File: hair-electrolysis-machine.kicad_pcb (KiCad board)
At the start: 2 copper layers, 53 x 53 mm, 84 parts, among them J1 USB_C_Receptacle_USB2.0_16P, J2 Conn_01x04_Pin, J3 AudioJack2_Ground_Switch, J4 AudioJack2_Ground_Switch, J5 Conn_01x04_Pin, J6 Conn_01x04_Pin, J7 AudioJack2_Ground_Switch, Q2 BSS138, SW3 SW_SPDT, SW4 RotaryEncoder_Switch, SW7 TRIGGER, SW8 TRIGGER, SW9 TRIGGER, U1 STM32G0B1RETx, U2 TP4054, U4 XC6206PxxxMR, U8 LM358B

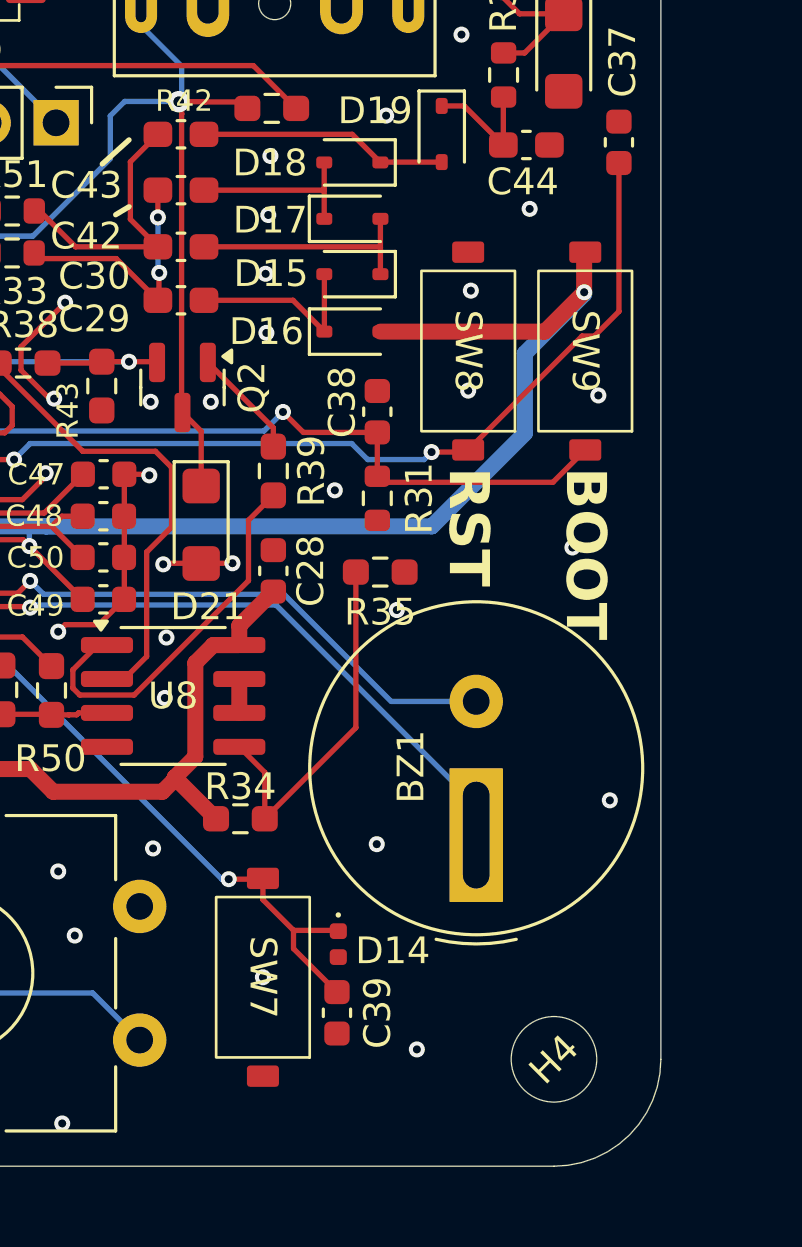
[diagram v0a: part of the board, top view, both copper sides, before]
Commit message: Fix C37 LCSC code, changed buttons to C720477
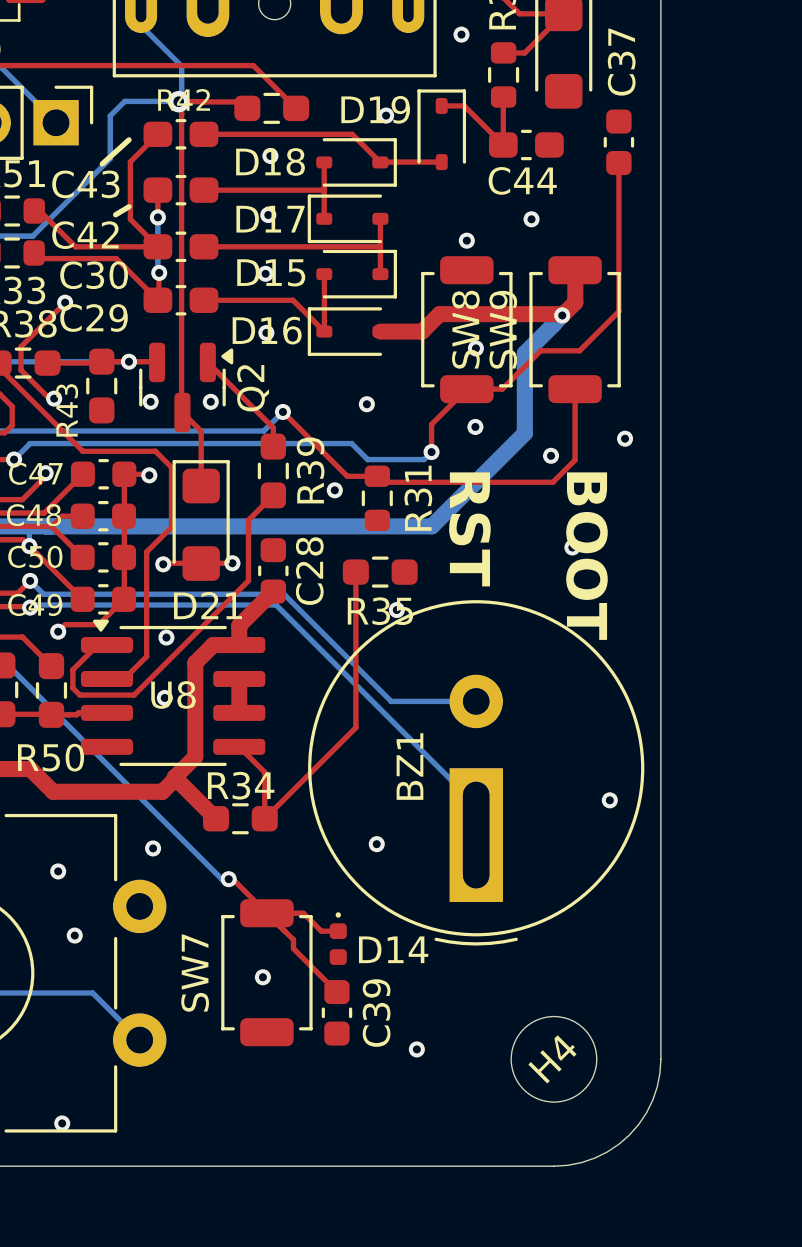
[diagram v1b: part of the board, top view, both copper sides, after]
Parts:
- removed C38: 100nF, Capacitor_SMD:C_0603_1608Metric
- SW7: footprint Button_Switch_SMD:YZA-032-5.0W -> Button_Switch_SMD:SW_SPST_TS-1088-xR025
- SW8: value TRIGGER -> RST; footprint Button_Switch_SMD:YZA-032-5.0W -> Button_Switch_SMD:SW_SPST_TS-1088-xR025
- SW9: value TRIGGER -> BOOT; footprint Button_Switch_SMD:YZA-032-5.0W -> Button_Switch_SMD:SW_SPST_TS-1088-xR025
- moved SW9 0.89 mm to (172.8, 92.7), turned to 90 degrees
- moved SW8 0.80 mm to (168.7, 92.7), turned to 90 degrees
- moved SW7 0.23 mm to (161.3, 116.8), turned to 90 degrees
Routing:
- net +3.3V: track 110.8 -> 108.8 mm
- net /Mcu/TRIGGER: track 66.0 -> 67.5 mm
- net SWCLK: track 51.5 -> 52.6 mm
- net /Mcu/~{RESET}: track 32.4 -> 33.0 mm
- net GND: vias 83 -> 86

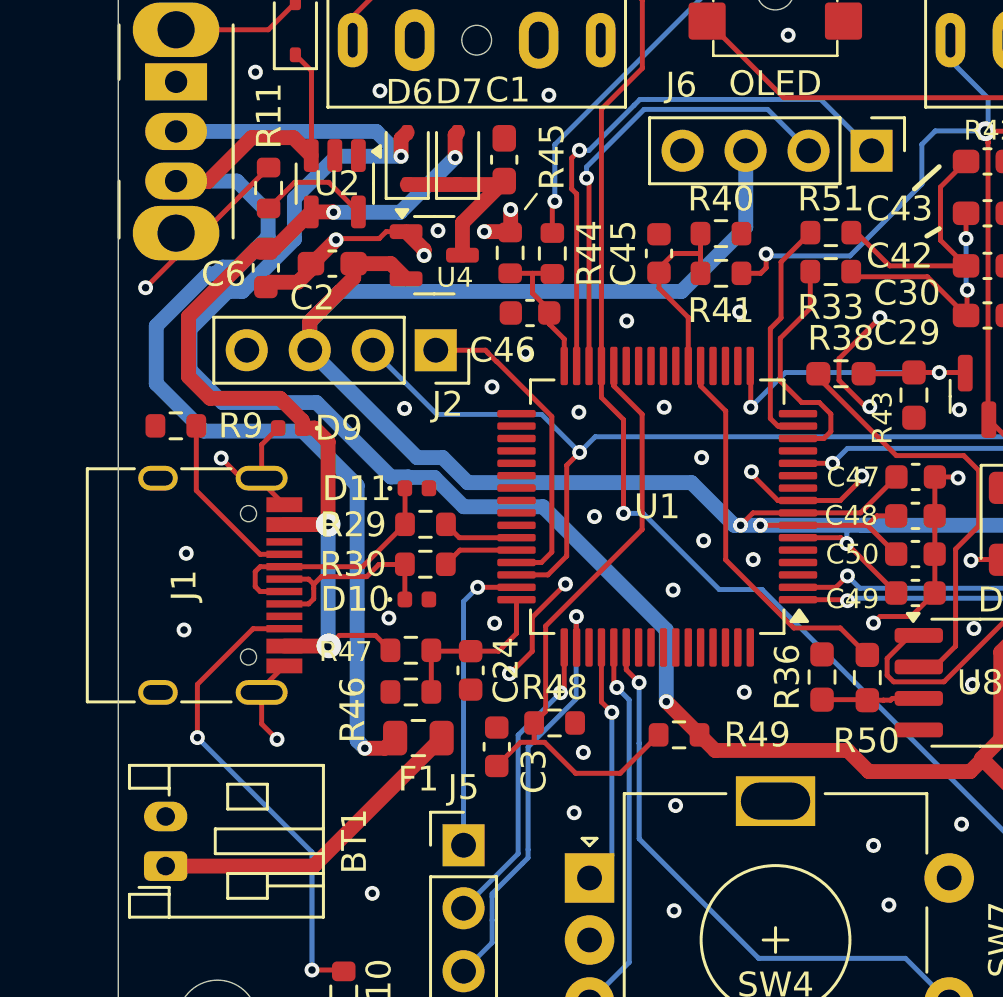
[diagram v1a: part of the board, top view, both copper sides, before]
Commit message: Removed USB resistors, shuffled breakout pins to tidy up a tad
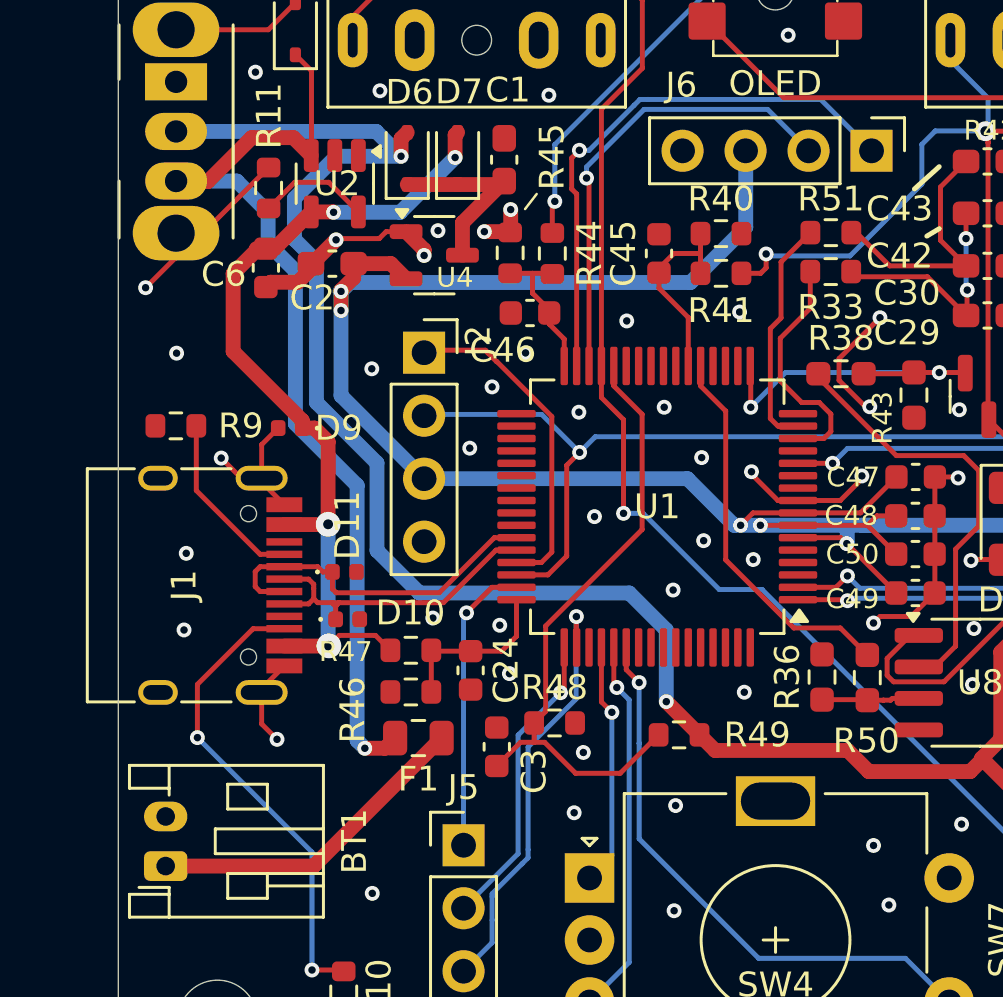
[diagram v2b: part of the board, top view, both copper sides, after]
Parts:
- removed R29, R30: 22R, Resistor_SMD:R_0603_1608Metric
- moved D11 4.46 mm to (132.1, 101.9)
- moved D10 2.90 mm to (132.2, 103.8)
- moved J2 0.48 mm to (135.3, 93.1), turned to 0 degrees
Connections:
- SW3 pad : GND -> (no net)
- U1 pad 43: Net-(U1-PA9/PA11) -> /Mcu/D-
- U1 pad 44: Net-(U1-PA10/PA12) -> /Mcu/D+
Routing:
- net Net-(D5-K): track 45.7 -> 39.1 mm
- net /Mcu/D+: track 8.56 -> 13.2 mm
- net GND: track 58.2 -> 53.6 mm, vias 86 -> 87
- net /Mcu/D-: track 10.2 -> 14.2 mm
- net +BATT: track 75.8 -> 71.8 mm
- net SWCLK: track 52.6 -> 49.5 mm
- net Net-(U1-PA10/PA12): track 3.09 -> 0.00 mm
- net Net-(U1-PA9/PA11): track 3.07 -> 0.00 mm
- net +3.3V: track 108.8 -> 106.0 mm, vias 4 -> 6
- net +5V: track 38.8 -> 36.0 mm
- net SWDIO: track 12.9 -> 13.4 mm

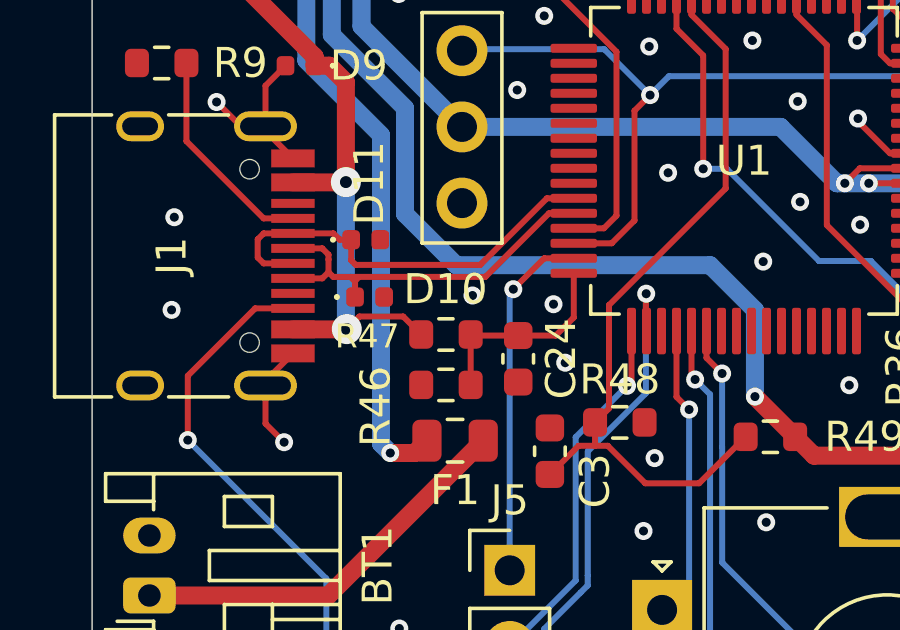
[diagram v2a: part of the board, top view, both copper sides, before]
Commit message: Forgot to ground switch housing. This WILL happen again.
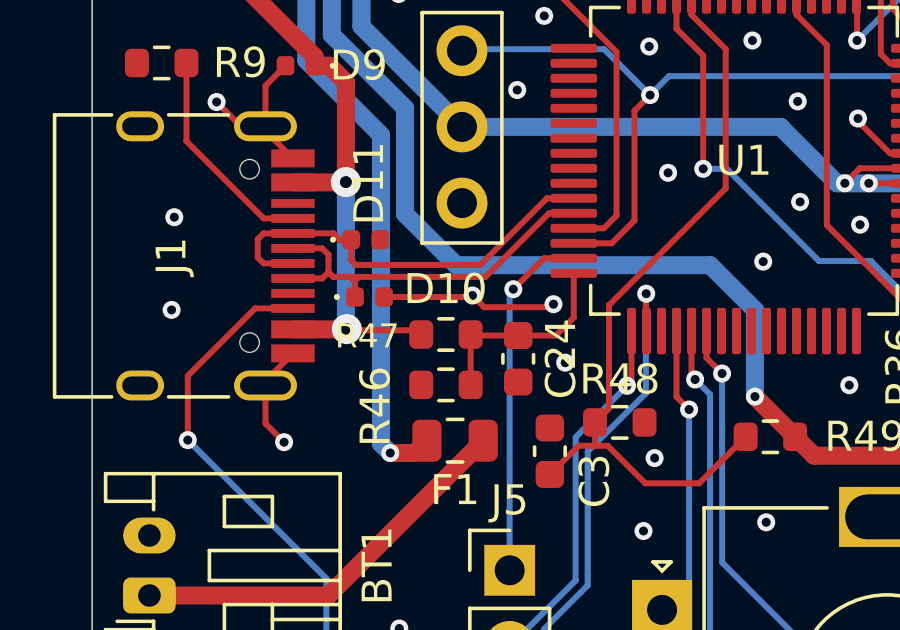
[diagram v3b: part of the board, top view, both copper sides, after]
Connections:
- SW3 pad : (no net) -> GND
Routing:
- net GND: track 53.6 -> 59.5 mm
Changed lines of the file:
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@@
 			(layers "*.Cu" "*.Mask")
 			(remove_unused_layers no)
+			(net "GND")
 		)
 		(pad "" thru_hole oval
@@
 			(layers "*.Cu" "*.Mask")
 			(remove_unused_layers no)
+			(net "GND")
 		)
 		(pad "1" thru_hole rect
@@
 	)
 	(segment
+		(start 136.07 104.19)
+		(end 138.28 104.19)
+		(width 0.2)
+		(layer "F.Cu")
+		(net "GND")
+	)
+	(segment
 		(start 133.52 88.5)
 		(end 133.8 88.22)
@@
 	)
 	(segment
+		(start 138.28 104.19)
+		(end 138.38 104.09)
+		(width 0.2)
+		(layer "F.Cu")
+		(net "GND")
+	)
+	(segment
+		(start 135.63 103.85)
+		(end 135.68 103.8)
+		(width 0.2)
+		(layer "F.Cu")
+		(net "GND")
+	)
+	(segment
 		(start 156.82 98.11)
 		(end 156.86 98.15)
@@
 	)
 	(segment
+		(start 132.735 103.85)
+		(end 135.63 103.85)
+		(width 0.2)
+		(layer "F.Cu")
+		(net "GND")
+	)
+	(segment
 		(start 152.11 99.06)
 		(end 150.405 99.06)
@@
 	)
 	(segment
+		(start 135.68 103.8)
+		(end 136.07 104.19)
+		(width 0.2)
+		(layer "F.Cu")
+		(net "GND")
+	)
+	(segment
 		(start 125.33 80.080001)
 		(end 129.049999 80.080001)
@@
 	)
 	(segment
-		(start 133.37 104.5)
+		(start 133.83 104.96)
 		(end 133.97 105.1)
 		(width 0.2)
@@
 	)
 	(segment
+		(start 131.48 104.93)
+		(end 131.51 104.96)
+		(width 0.2)
+		(layer "F.Cu")
+		(net "+5V")
+	)
+	(segment
 		(start 128.565 88.905)
 		(end 128.95 88.905)
@@
 	)
 	(segment
-		(start 131.91 104.5)
-		(end 133.37 104.5)
-		(width 0.2)
-		(layer "F.Cu")
-		(net "+5V")
-	)
-	(segment
 		(start 128.95 88.905)
 		(end 129.3 88.905)
@@
 	)
 	(segment
-		(start 129.3 88.905)
-		(end 130.78 87.425)
-		(width 0.6)
+		(start 131.51 104.96)
+		(end 133.83 104.96)
+		(width 0.2)
 		(layer "F.Cu")
 		(net "+5V")
 	)
 	(segment
-		(start 131.48 104.93)
-		(end 131.91 104.5)
-		(width 0.2)
+		(start 129.3 88.905)
+		(end 130.78 87.425)
+		(width 0.6)
 		(layer "F.Cu")
 		(net "+5V")

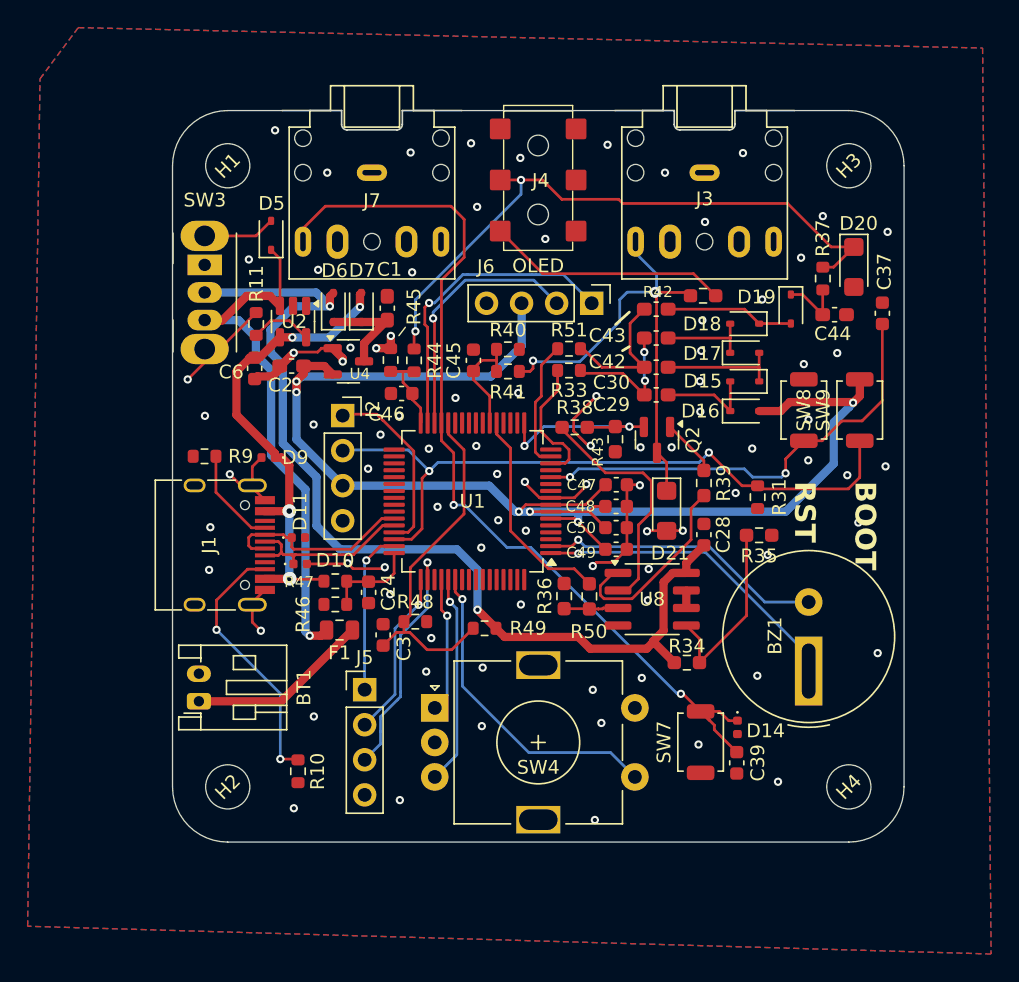
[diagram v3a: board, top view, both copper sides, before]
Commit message: Silkscreen fixes
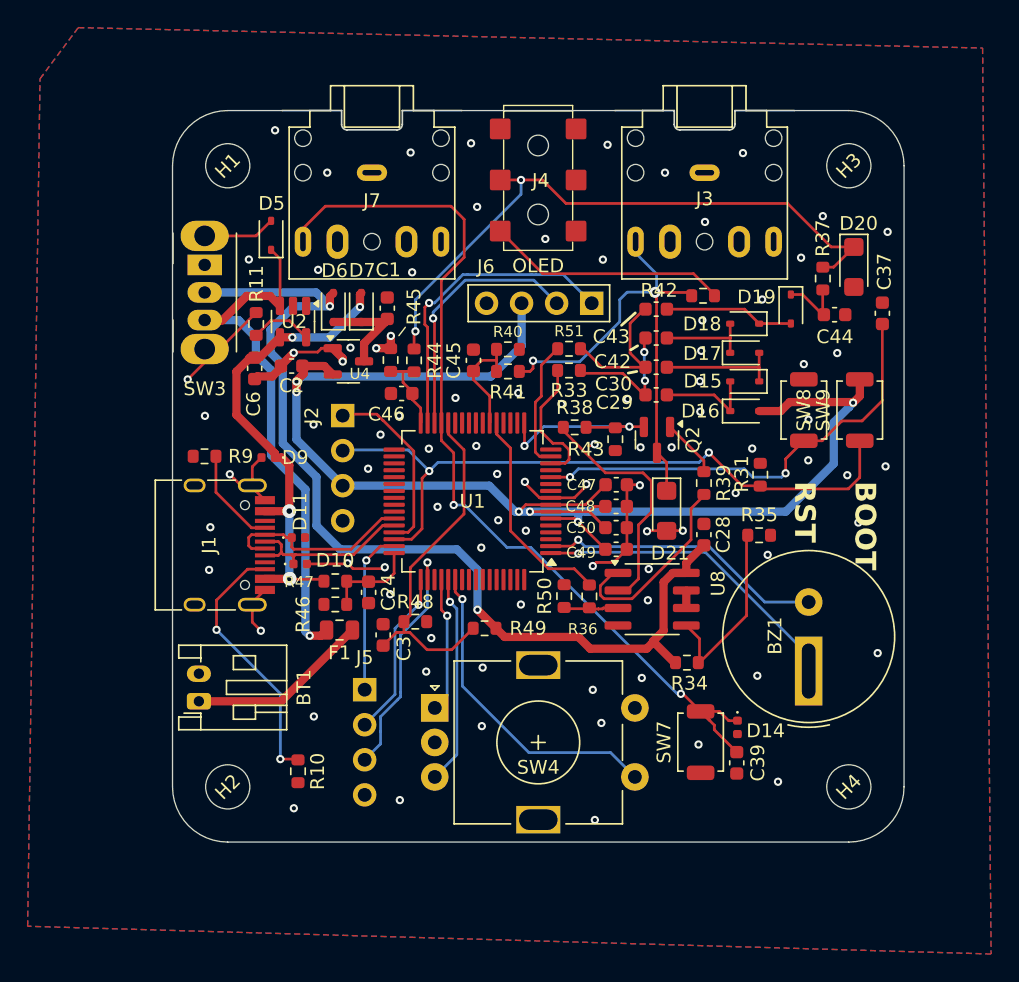
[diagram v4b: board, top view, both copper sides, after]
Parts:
- C1, C2, C29, C30, C42, C43, C44: footprint Capacitor_SMD:C_0603_1608Metric_Pad1.08x0.95mm_HandSolder -> Capacitor_SMD:C_0603_1608Metric
- R34, R35, R36, R38, R39, R42, R43, R50: footprint Resistor_SMD:R_0603_1608Metric_Pad0.98x0.95mm_HandSolder -> Resistor_SMD:R_0603_1608Metric
- moved G*** 3.77 mm to (150.3, 99.0)
- moved R31 1.64 mm to (165.6, 97.4), turned to 90 degrees
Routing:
- net GND: track 59.5 -> 55.1 mm, vias 87 -> 88
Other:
- board text added: "- 3v3"
- board text added: "- GND"
- board text added: "- SWCLK"
- board text added: "- SWDIO"
- board text removed: "3v3"
- board text removed: "GND"
- board text removed: "SWCLK"
- board text removed: "SWDIO"

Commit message: Use STM32G0B1RBTx, fix up some silkscreen, maybe production ready?
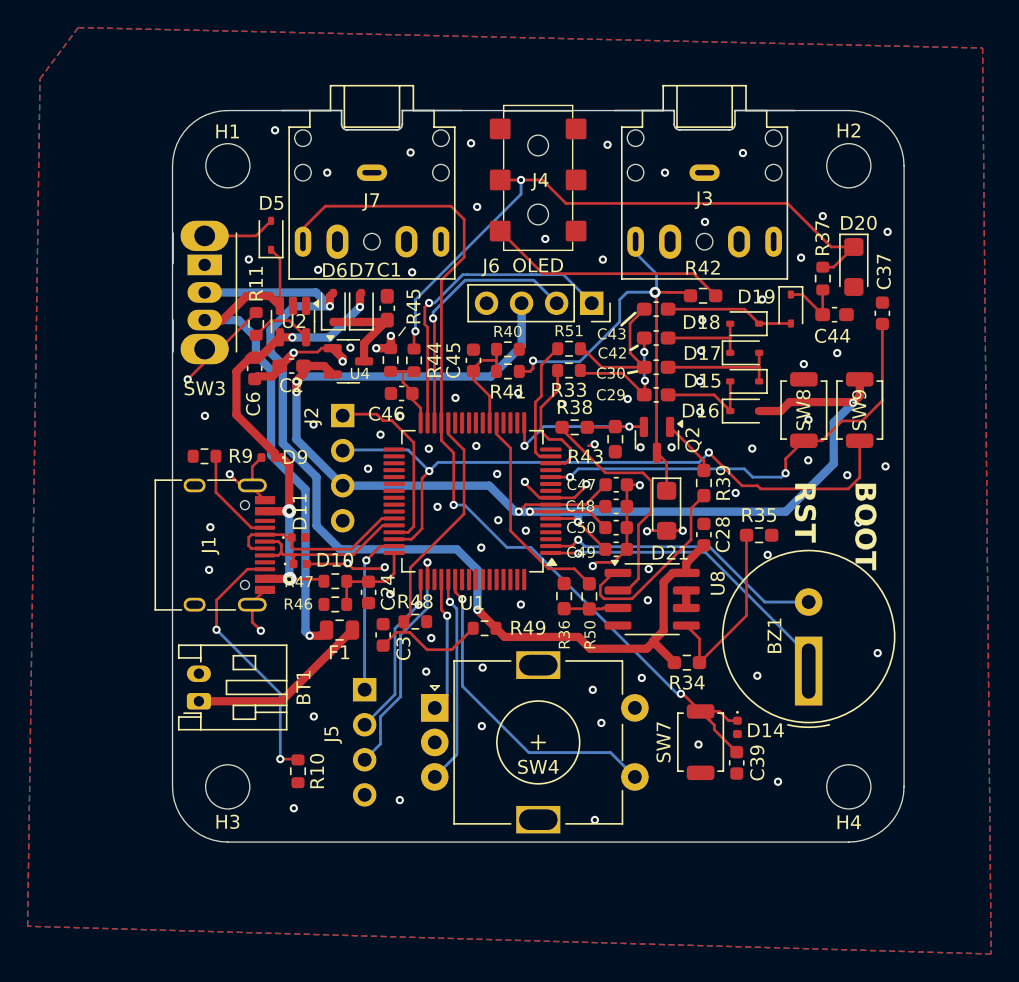
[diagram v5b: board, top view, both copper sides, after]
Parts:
- removed R31: 10K, Resistor_SMD:R_0603_1608Metric
- C1, C2, C29, C30, C42, C43, C44: footprint Capacitor_SMD:C_0603_1608Metric -> Capacitor_SMD:C_0603_1608Metric_Pad1.08x0.95mm_HandSolder
- H1, H2, H3, H4: value MountingHole_Pad -> MountingHole
- J6: footprint Connector_PinHeader_2.54mm:PinHeader_1x04_P2.54mm_Vertical -> Connector_PinSocket_2.54mm:PinSocket_1x04_P2.54mm_Vertical
- R34, R35: value 100K -> 100K1%; footprint Resistor_SMD:R_0603_1608Metric -> Resistor_SMD:R_0603_1608Metric_Pad0.98x0.95mm_HandSolder
- R36, R38, R39, R42, R43, R50: footprint Resistor_SMD:R_0603_1608Metric -> Resistor_SMD:R_0603_1608Metric_Pad0.98x0.95mm_HandSolder
- SW7: value TRIGGER -> BTN
- SW8: value RST -> BTN
- SW9: value BOOT -> BTN
- U1: value STM32G0B1RETx -> STM32G0B1RBTx
- moved H2 63.6 mm to (172.0, 75.0), turned to 0 degrees
- moved H3 63.6 mm to (127.0, 120.0), turned to 0 degrees
- turned H1 to 0 degrees
- turned H4 to 0 degrees
